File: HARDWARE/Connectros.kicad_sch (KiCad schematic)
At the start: 7 parts, among them J4 Sygnały, J5 Diagnostyka, J8 Zasilanie+CAN

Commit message: Align components on the PCB
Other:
- company: (none) -> PUT Motorsport
- moved on the sheet: J4, J5, R15, R17

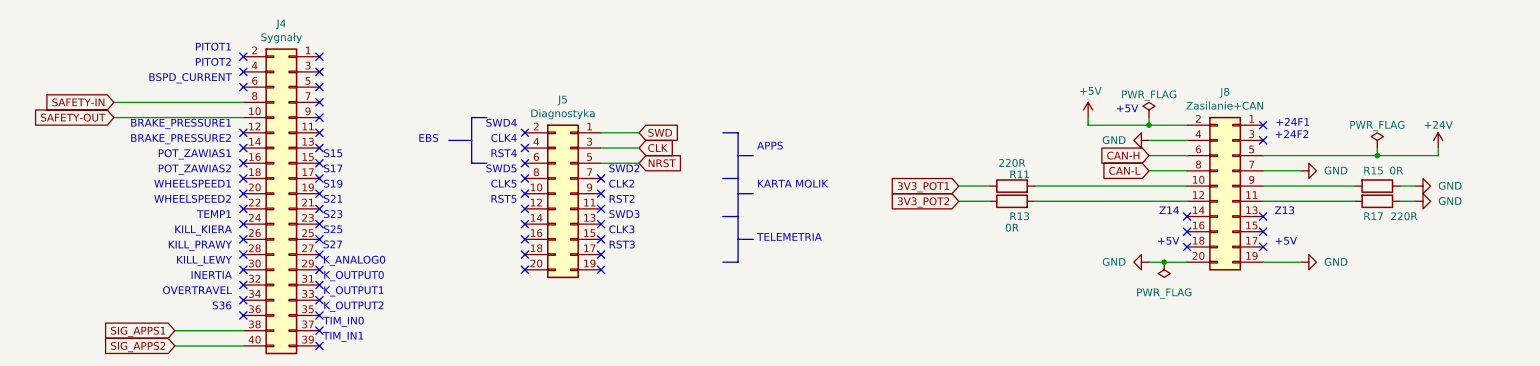
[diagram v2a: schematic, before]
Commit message: Route PCB tracks
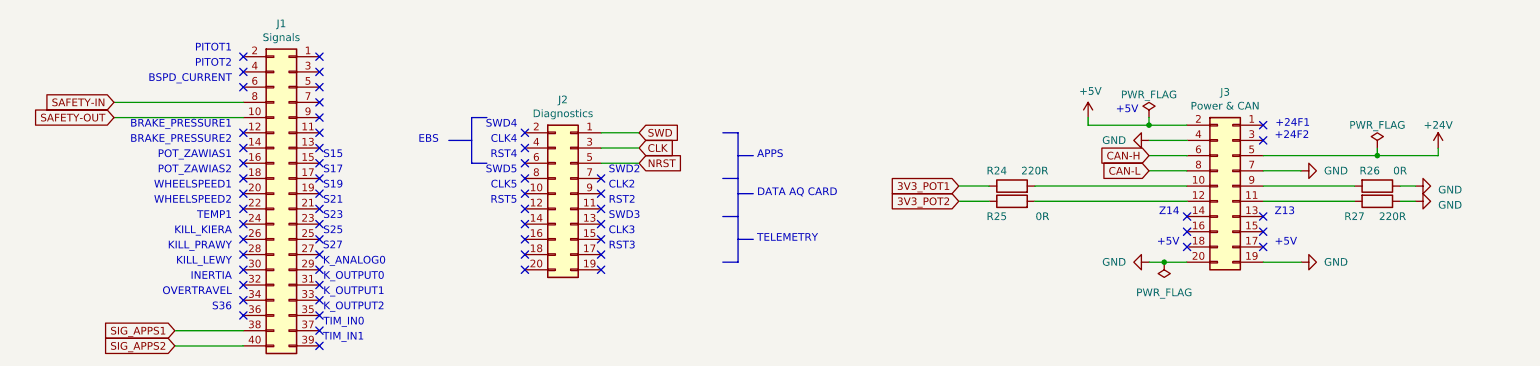
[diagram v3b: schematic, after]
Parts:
- J1: renamed from J4; value Sygnały -> Signals
- J2: renamed from J5; value Diagnostyka -> Diagnostics
- J3: renamed from J8; value Zasilanie+CAN -> Power & CAN
- renumbered R11 to R24, R13 to R25, R15 to R26, R17 to R27
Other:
- note added: "DATA AQ CARD"
- note added: "TELEMETRY"
- note removed: "KARTA MOLIK"
- note removed: "TELEMETRIA"
- company: PUT Motorsport -> S. Sambor
- title: (none) -> Connectors
